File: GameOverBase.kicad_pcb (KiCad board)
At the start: 4 copper layers, 50 x 35 mm, 47 parts, among them J1 USB_C_DEALON-USB-US31-106, J2 Serial Port, J3 add-on conn, Q1 PMN48XP, SW1 SW_DIP_x08, SW2 boot, SW3 Reset, U1 ESP32-WROOM-E, U2 4021, U3 MCP73831-2ACI-OT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

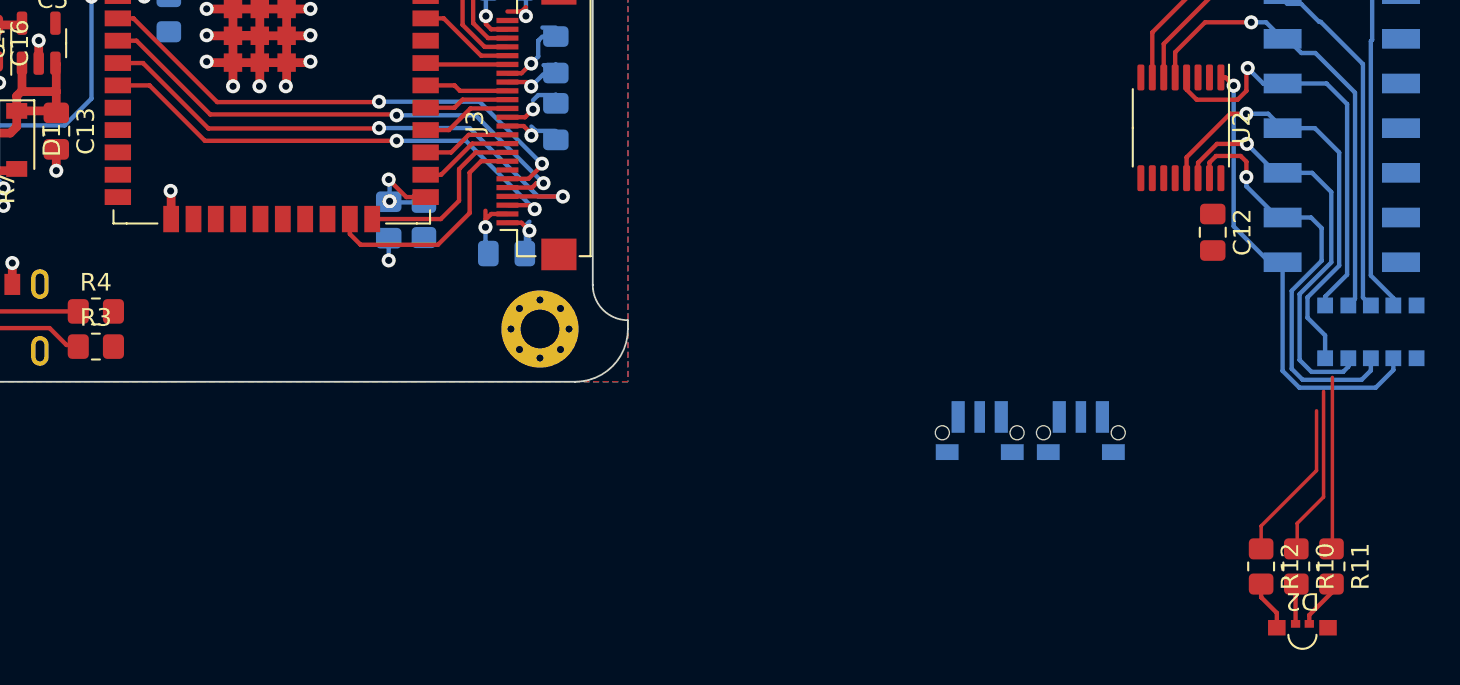
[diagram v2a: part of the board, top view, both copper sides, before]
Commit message: Routes RGB led
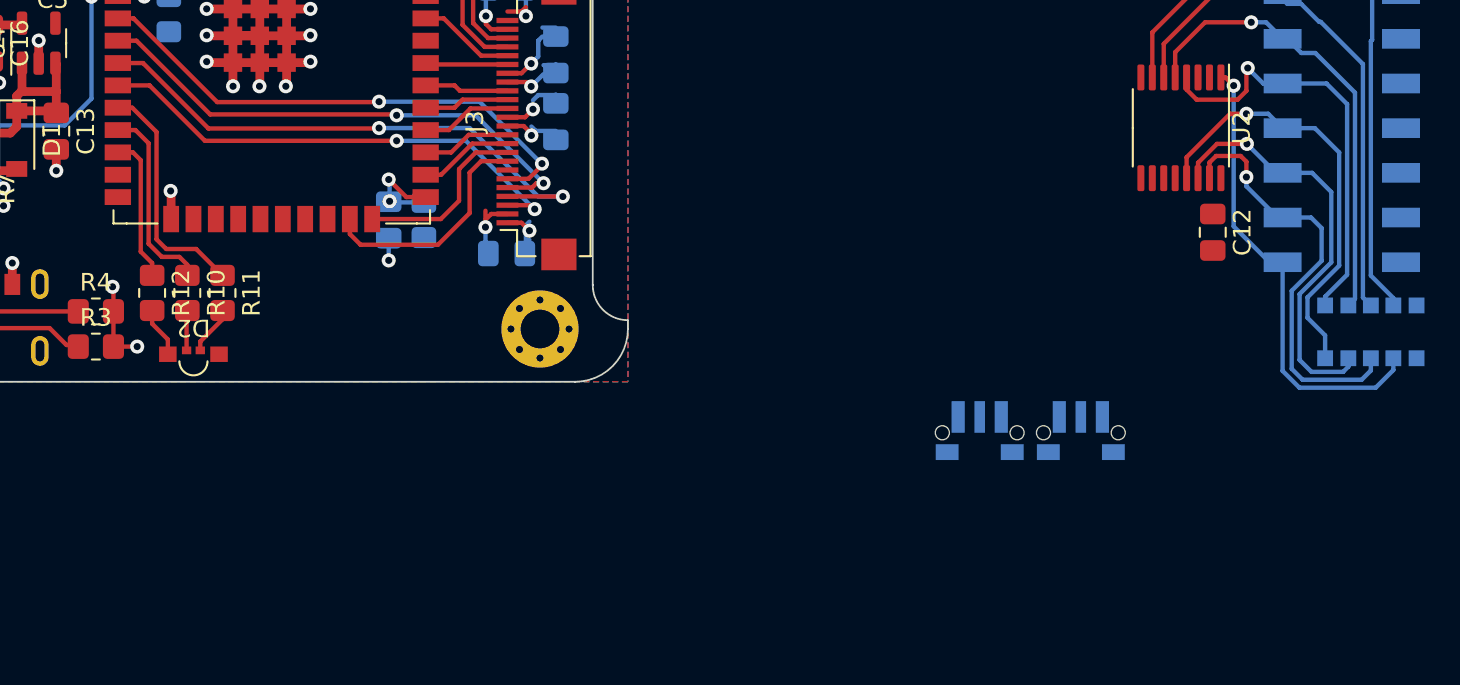
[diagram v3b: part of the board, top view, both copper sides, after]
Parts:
- moved R10 64.9 mm to (144.9, 110.0)
- moved R11 64.9 mm to (146.9, 110.0)
- moved R12 64.9 mm to (142.9, 110.0)
- moved D2 64.9 mm to (145.3, 113.4)
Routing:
- net GND: track 84.5 -> 89.3 mm, vias 36 -> 38
- net BAT_IND_G: track 9.77 -> 13.5 mm
- net BAT_IND_R: track 9.59 -> 11.1 mm
- net BAT_IND_B: track 9.15 -> 8.30 mm
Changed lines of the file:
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@@
   )
   (footprint "Resistor_SMD:R_0805_2012Metric_Pad1.20x1.40mm_HandSolder" (layer "F.Cu")
-    (at 208 125.5 -90)
+    (at 144.95 109.95 -90)
     (descr "Resistor SMD 0805 (2012 Metric), square (rectangular) end terminal, IPC_7351 nominal with elongated pad for handsoldering. (Body size source: IPC-SM-782 page 72, https://www.pcb-3d.com/wordpress/wp-content/uploads/ipc-sm-782a_amendment_1_and_2.pdf), generated with kicad-footprint-generator")
     (tags "resistor handsolder")
@@
   )
   (footprint "Resistor_SMD:R_0805_2012Metric_Pad1.20x1.40mm_HandSolder" (layer "F.Cu")
-    (at 206 125.5 -90)
+    (at 142.95 109.95 -90)
     (descr "Resistor SMD 0805 (2012 Metric), square (rectangular) end terminal, IPC_7351 nominal with elongated pad for handsoldering. (Body size source: IPC-SM-782 page 72, https://www.pcb-3d.com/wordpress/wp-content/uploads/ipc-sm-782a_amendment_1_and_2.pdf), generated with kicad-footprint-generator")
     (tags "resistor handsolder")
@@
   )
   (footprint "Resistor_SMD:R_0805_2012Metric_Pad1.20x1.40mm_HandSolder" (layer "F.Cu")
-    (at 210 125.5 -90)
+    (at 146.95 109.95 -90)
     (descr "Resistor SMD 0805 (2012 Metric), square (rectangular) end terminal, IPC_7351 nominal with elongated pad for handsoldering. (Body size source: IPC-SM-782 page 72, https://www.pcb-3d.com/wordpress/wp-content/uploads/ipc-sm-782a_amendment_1_and_2.pdf), generated with kicad-footprint-generator")
     (tags "resistor handsolder")
@@
   )
   (footprint "GameOver:Hongzhi_Forest_HS-1204-RGB" (layer "F.Cu")
-    (at 208.3475 128.984368 180)
+    (at 145.2975 113.434368 180)
     (property "Sheetfile" "GameOverBase.kicad_sch")
     (property "Sheetname" "")
@@
   (segment (start 138.7 87.6) (end 138.7 87.1625) (width 0.5) (layer "F.Cu") (net 2))
   (segment (start 144.03 104.18) (end 144 104.15) (width 0.5) (layer "F.Cu") (net 2))
+  (segment (start 140.75 109.65) (end 140.7 109.6) (width 0.25) (layer "F.Cu") (net 2))
   (segment (start 133 105) (end 134.5 105) (width 0.5) (layer "F.Cu") (net 2))
   (segment (start 149.05 98.2) (end 149.07 98.18) (width 0.5) (layer "F.Cu") (net 2))
@@
   (segment (start 150.55 98.2) (end 150.595 98.155) (width 0.5) (layer "F.Cu") (net 2))
   (segment (start 128.75 96.75) (end 129.4625 96.75) (width 0.5) (layer "F.Cu") (net 2))
+  (segment (start 140.75 111) (end 140.75 109.65) (width 0.25) (layer "F.Cu") (net 2))
   (segment (start 147.55 98.2) (end 147.545 98.195) (width 0.5) (layer "F.Cu") (net 2))
   (segment (start 147.545 93.805) (end 147.545 92.405) (width 0.5) (layer "F.Cu") (net 2))
   (segment (start 147.545 95.33) (end 146.08 95.33) (width 0.5) (layer "F.Cu") (net 2))
   (segment (start 147.545 95.33) (end 147.545 93.805) (width 0.5) (layer "F.Cu") (net 2))
+  (segment (start 140.75 113) (end 140.75 111) (width 0.25) (layer "F.Cu") (net 2))
   (segment (start 147.545 96.855) (end 147.545 95.33) (width 0.5) (layer "F.Cu") (net 2))
   (segment (start 147.545 96.855) (end 146.105 96.855) (width 0.5) (layer "F.Cu") (net 2))
+  (segment (start 140.75 113) (end 142.1 113) (width 0.25) (layer "F.Cu") (net 2))
   (segment (start 151.95 93.8) (end 151.945 93.805) (width 0.5) (layer "F.Cu") (net 2))
   (segment (start 151.92 95.33) (end 151.95 95.3) (width 0.5) (layer "F.Cu") (net 2))
@@
   (via (at 137.5 103) (size 0.8) (drill 0.4) (layers "F.Cu" "B.Cu") (net 2))
   (via (at 124.5 104.5) (size 0.8) (drill 0.4) (layers "F.Cu" "B.Cu") (net 2))
+  (via (at 142.1 113) (size 0.8) (drill 0.4) (layers "F.Cu" "B.Cu") (net 2))
   (via (at 146.05 96.8) (size 0.8) (drill 0.4) (layers "F.Cu" "B.Cu") (net 2))
   (via (at 164.5 96.91) (size 0.8) (drill 0.4) (layers "F.Cu" "B.Cu") (net 2))
@@
   (via (at 147.55 92.4) (size 0.8) (drill 0.4) (layers "F.Cu" "B.Cu") (net 2))
   (via (at 122.9 94.8) (size 0.8) (drill 0.4) (layers "F.Cu" "B.Cu") (net 2))
+  (via (at 140.7 109.6) (size 0.8) (drill 0.4) (layers "F.Cu" "B.Cu") (net 2))
   (via (at 164.6 99.51) (size 0.8) (drill 0.4) (layers "F.Cu" "B.Cu") (net 2))
   (via (at 134.25 98) (size 0.8) (drill 0.4) (layers "F.Cu" "B.Cu") (net 2))
@@
   (segment (start 130.5 102) (end 130.75 101.75) (width 0.5) (layer "F.Cu") (net 10))
   (segment (start 135.15 103) (end 135.25 102.9) (width 0.5) (layer "F.Cu") (net 10))
-  (segment (start 207.9575 128.764368) (end 207.9575 126.5425) (width 0.25) (layer "F.Cu") (net 11))
-  (segment (start 207.9575 126.5425) (end 208 126.5) (width 0.25) (layer "F.Cu") (net 11))
-  (segment (start 208.7375 128.764368) (end 208.7375 128.2625) (width 0.25) (layer "F.Cu") (net 12))
-  (segment (start 210 127) (end 210 126.5) (width 0.25) (layer "F.Cu") (net 12))
-  (segment (start 208.7375 128.2625) (end 210 127) (width 0.25) (layer "F.Cu") (net 12))
-  (segment (start 206 127.25) (end 206.8925 128.1425) (width 0.25) (layer "F.Cu") (net 13))
-  (segment (start 206 126.5) (end 206 127.25) (width 0.25) (layer "F.Cu") (net 13))
-  (segment (start 206.8925 128.1425) (end 206.8925 128.984368) (width 0.25) (layer "F.Cu") (net 13))
+  (segment (start 144.9075 113.214368) (end 144.9075 110.9925) (width 0.25) (layer "F.Cu") (net 11))
+  (segment (start 144.9075 110.9925) (end 144.95 110.95) (width 0.25) (layer "F.Cu") (net 11))
+  (segment (start 145.6875 113.214368) (end 145.6875 112.7125) (width 0.25) (layer "F.Cu") (net 12))
+  (segment (start 146.95 111.45) (end 146.95 110.95) (width 0.25) (layer "F.Cu") (net 12))
+  (segment (start 145.6875 112.7125) (end 146.95 111.45) (width 0.25) (layer "F.Cu") (net 12))
+  (segment (start 142.95 111.7) (end 143.8425 112.5925) (width 0.25) (layer "F.Cu") (net 13))
+  (segment (start 142.95 110.95) (end 142.95 111.7) (width 0.25) (layer "F.Cu") (net 13))
+  (segment (start 143.8425 112.5925) (end 143.8425 113.434368) (width 0.25) (layer "F.Cu") (net 13))
   (segment (start 142.5 93.1) (end 142.47 93.07) (width 0.25) (layer "F.Cu") (net 14))
   (segment (start 129.276069 100.95) (end 127.3875 100.95) (width 0.25) (layer "F.Cu") (net 14))
@@
   (segment (start 125.0625 101) (end 125.1125 100.95) (width 0.5) (layer "F.Cu") (net 42))
   (segment (start 123 101) (end 125.0625 101) (width 0.5) (layer "F.Cu") (net 42))
-  (segment (start 209.55 121.55) (end 209.55 115.55) (width 0.2) (layer "F.Cu") (net 43))
-  (segment (start 208 124.5) (end 208.05 124.45) (width 0.2) (layer "F.Cu") (net 43))
-  (segment (start 208.05 123.05) (end 209.55 121.55) (width 0.2) (layer "F.Cu") (net 43))
-  (segment (start 208.05 124.45) (end 208.05 123.05) (width 0.2) (layer "F.Cu") (net 43))
-  (segment (start 210.05 124.45) (end 210.05 114.75) (width 0.2) (layer "F.Cu") (net 44))
-  (segment (start 210 124.5) (end 210.05 124.45) (width 0.2) (layer "F.Cu") (net 44))
-  (segment (start 209.15 116.65) (end 209.15 120.05) (width 0.2) (layer "F.Cu") (net 45))
-  (segment (start 206 123.2) (end 206 124.5) (width 0.2) (layer "F.Cu") (net 45))
-  (segment (start 209.15 120.05) (end 206 123.2) (width 0.2) (layer "F.Cu") (net 45))
+  (segment (start 142.75048 107.15048) (end 143.5 107.9) (width 0.25) (layer "F.Cu") (net 43))
+  (segment (start 141 100.69) (end 142 100.69) (width 0.25) (layer "F.Cu") (net 43))
+  (segment (start 142 100.69) (end 142.75048 101.44048) (width 0.25) (layer "F.Cu") (net 43))
+  (segment (start 144.95 108.35) (end 144.95 108.95) (width 0.25) (layer "F.Cu") (net 43))
+  (segment (start 144.5 107.9) (end 144.95 108.35) (width 0.25) (layer "F.Cu") (net 43))
+  (segment (start 143.5 107.9) (end 144.5 107.9) (width 0.25) (layer "F.Cu") (net 43))
+  (segment (start 142.75048 101.44048) (end 142.75048 107.15048) (width 0.25) (layer "F.Cu") (net 43))
+  (segment (start 141.82 99.42) (end 143.2 100.8) (width 0.25) (layer "F.Cu") (net 44))
+  (segment (start 143.2 106.9) (end 143.75048 107.45048) (width 0.25) (layer "F.Cu") (net 44))
+  (segment (start 141 99.42) (end 141.82 99.42) (width 0.25) (layer "F.Cu") (net 44))
+  (segment (start 143.75048 107.45048) (end 145.45048 107.45048) (width 0.25) (layer "F.Cu") (net 44))
+  (segment (start 145.45048 107.45048) (end 146.95 108.95) (width 0.25) (layer "F.Cu") (net 44))
+  (segment (start 143.2 100.8) (end 143.2 106.9) (width 0.25) (layer "F.Cu") (net 44))
+  (segment (start 142.95 108.95) (end 142.95 108.25) (width 0.25) (layer "F.Cu") (net 45))
+  (segment (start 141.86 101.96) (end 141 101.96) (width 0.25) (layer "F.Cu") (net 45))
+  (segment (start 142.30096 107.60096) (end 142.30096 102.40096) (width 0.25) (layer "F.Cu") (net 45))
+  (segment (start 142.30096 102.40096) (end 141.86 101.96) (width 0.25) (layer "F.Cu") (net 45))
+  (segment (start 142.95 108.25) (end 142.30096 107.60096) (width 0.25) (layer "F.Cu") (net 45))
   (zone (net 0) (net_name "") (layers "F.Cu" "In1.Cu" "In2.Cu" "B.Cu") (name "Antenna_keepout") (hatch edge 0.508)
     (connect_pads (clearance 0))
